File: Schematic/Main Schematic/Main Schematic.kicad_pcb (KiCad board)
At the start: 2 copper layers, 100 x 100 mm, 56 parts, among them IC1 DW01A-G, IC2 LM75AD,118, J1 Conn_01x24_Socket, J11 Conn_01x09_Pin, J2 Conn_01x02_Pin, J3 Conn_01x24_Socket, J4 Conn_01x02_Male, J5 Conn_01x02_Male, J6 USB_B_Micro, J7 Conn_01x02_Pin, J8 Conn_01x24_Pin, J9 Conn_01x24_Pin, Q1 FS8205A, SW1 SW_Push, U1 HT75xx-1-SOT89, U2 MCP73831-2-OT, U3 CH340C, U4 M24C16-RMN6TP

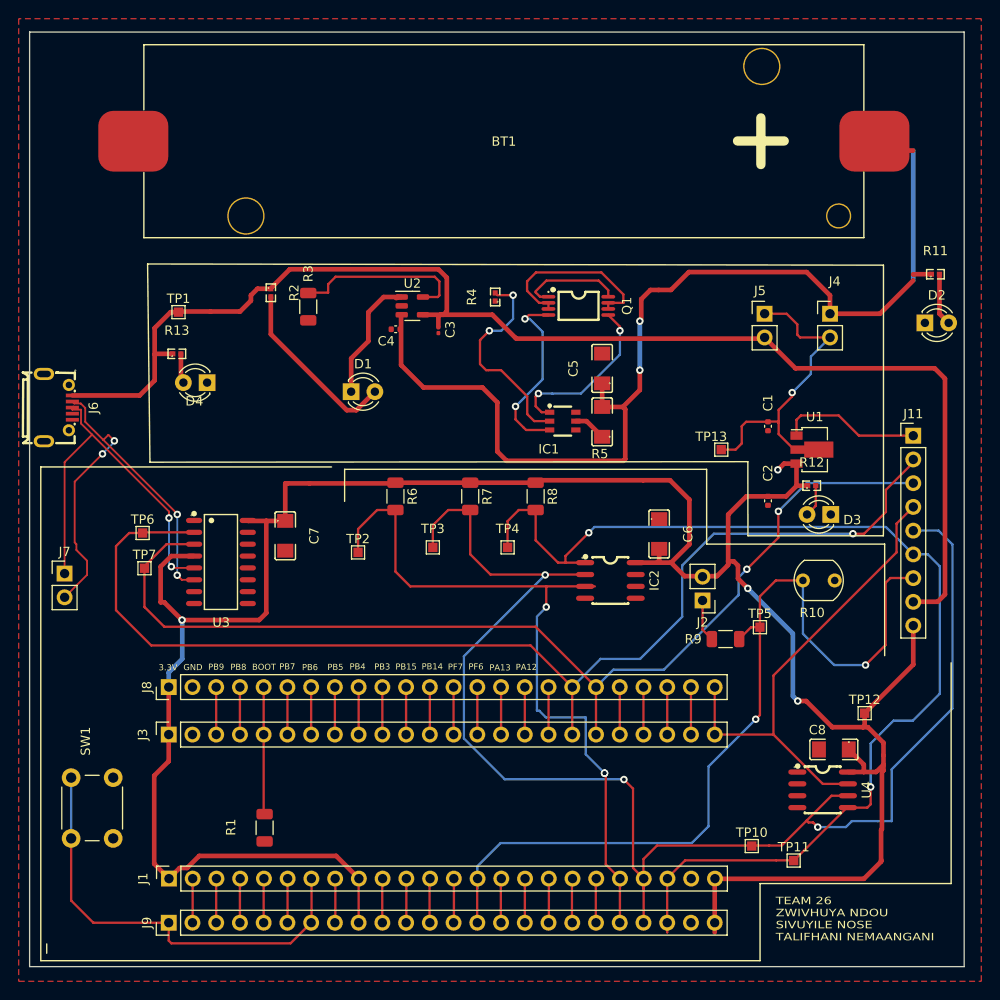
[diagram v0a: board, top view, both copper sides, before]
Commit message: Added silk screens on the PCB layout board
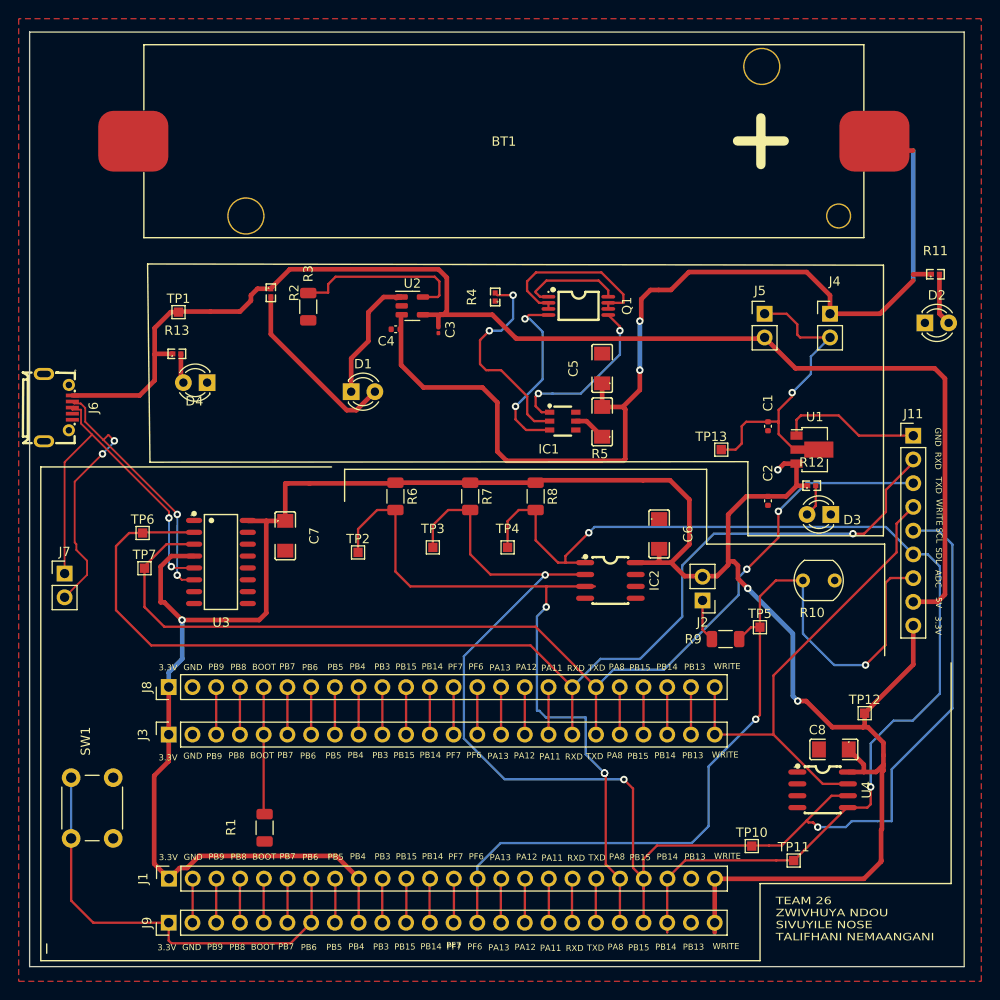
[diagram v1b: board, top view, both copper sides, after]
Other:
- board text added: "5V"
- board text added: "ADC"
- board text added: "PA11"
- board text added: "PA8"
- board text added: "PB13"
- board text added: "RXD"
- board text added: "SCL"
- board text added: "SDL"
- board text added: "TXD"
- board text added: "WRITE"

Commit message: Added UCT logo
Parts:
- added G***: LOGO, SilkSreen:UCT_LOGO, B.Cu at (151.6, 76.3)

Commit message: Edit
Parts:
- moved G*** 27.6 mm to (128.3, 90.9)
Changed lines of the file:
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@@
   )
   (footprint "SilkSreen:UCT_LOGO" (layer "B.Cu")
-    (at 151.62 76.27 180)
+    (at 128.27 90.93 180)
     (attr board_only exclude_from_pos_files exclude_from_bom)
-    (fp_text reference "G***" (at 0 0) (layer "B.SilkS")
+    (fp_text reference "G***" (at 0 0) (layer "B.SilkS") hide
         (effects (font (size 1.5 1.5) (thickness 0.3)) (justify mirror))
     )

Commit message: Design done
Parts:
- removed D2: LED, LED_THT:LED_D3.0mm
- removed R11: 1k, Local_Footprints:R0402
- CH340C UART: renamed from U3
- moved G*** 26.3 mm to (154.4, 93.4)
- renumbered U2 to BATTERY_CHARGER, J11 to DEBUGGER, C8 to EEPROM, IC1 to UVL_PRO, U1 to VOLT-DIV
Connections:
- J1 pad 8: Net-(J1-Pin_8) -> GND
- J9 pad 8: Net-(J1-Pin_8) -> GND
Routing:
- net Net-(D2-A): track 5.62 -> 0.00 mm
- net Net-(J1-Pin_8): track 4.65 -> 0.00 mm
- net GND: track 34.6 -> 39.2 mm
- net /Power Unit/V1: track 115.1 -> 113.1 mm
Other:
- board text added: "NSRT"
- board text added: "OS"
- board text added: "PA0"
- board text added: "PA1"
- board text added: "PA2"
- board text added: "PA3"
- board text added: "PA5"
- board text added: "PA6"
- board text added: "PA7"
- board text added: "PB0"
- board text added: "PB1"
- board text added: "PC14"
- board text added: "PF0"
- board text added: "PF1"
